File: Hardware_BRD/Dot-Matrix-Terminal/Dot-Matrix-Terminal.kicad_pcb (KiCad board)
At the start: 2 copper layers, 105 x 50 mm, 62 parts, among them J1 USB_B, J2 Conn_01x17, J3 Conn_01x10, J4 Conn_01x02, J5 Barrel_Jack, J6 Conn_01x02, J7 Conn_01x02, J8 Conn_01x02, Q1 IRLML0030, Q10 IRLML0030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

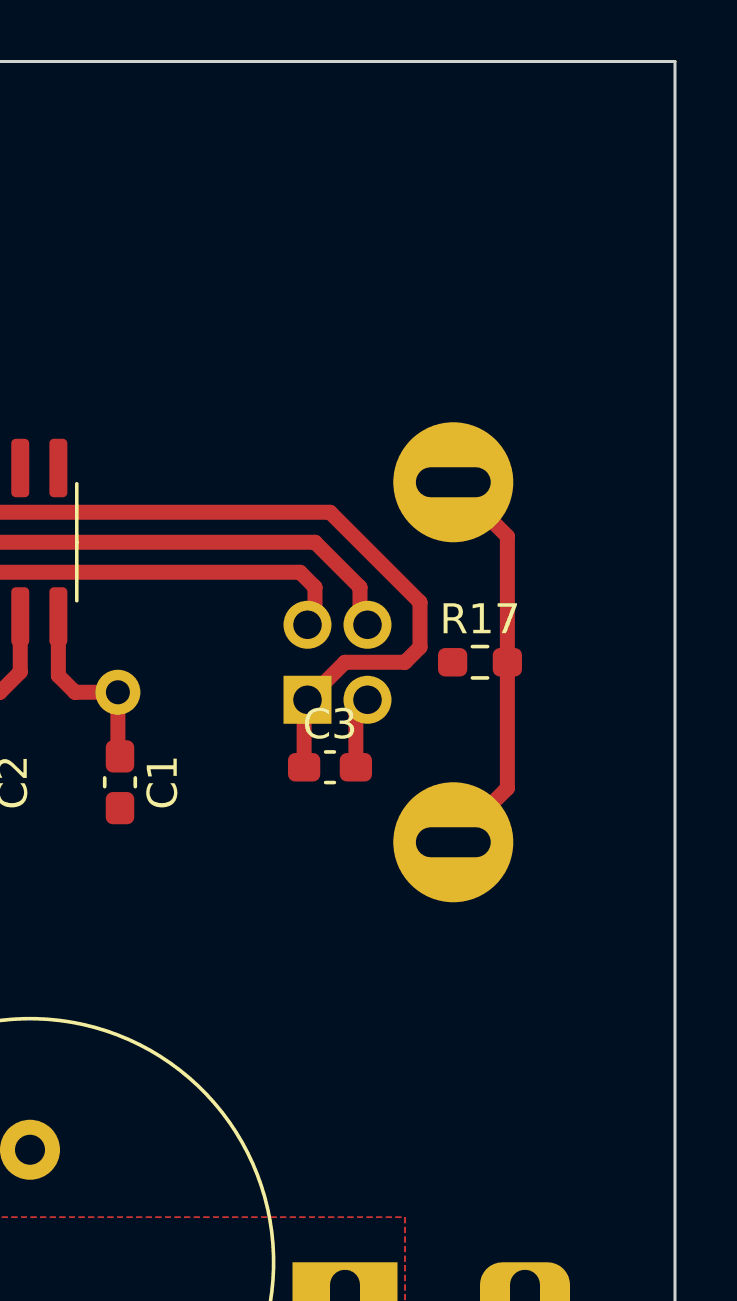
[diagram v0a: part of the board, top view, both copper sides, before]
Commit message: Couple of mounting holes added
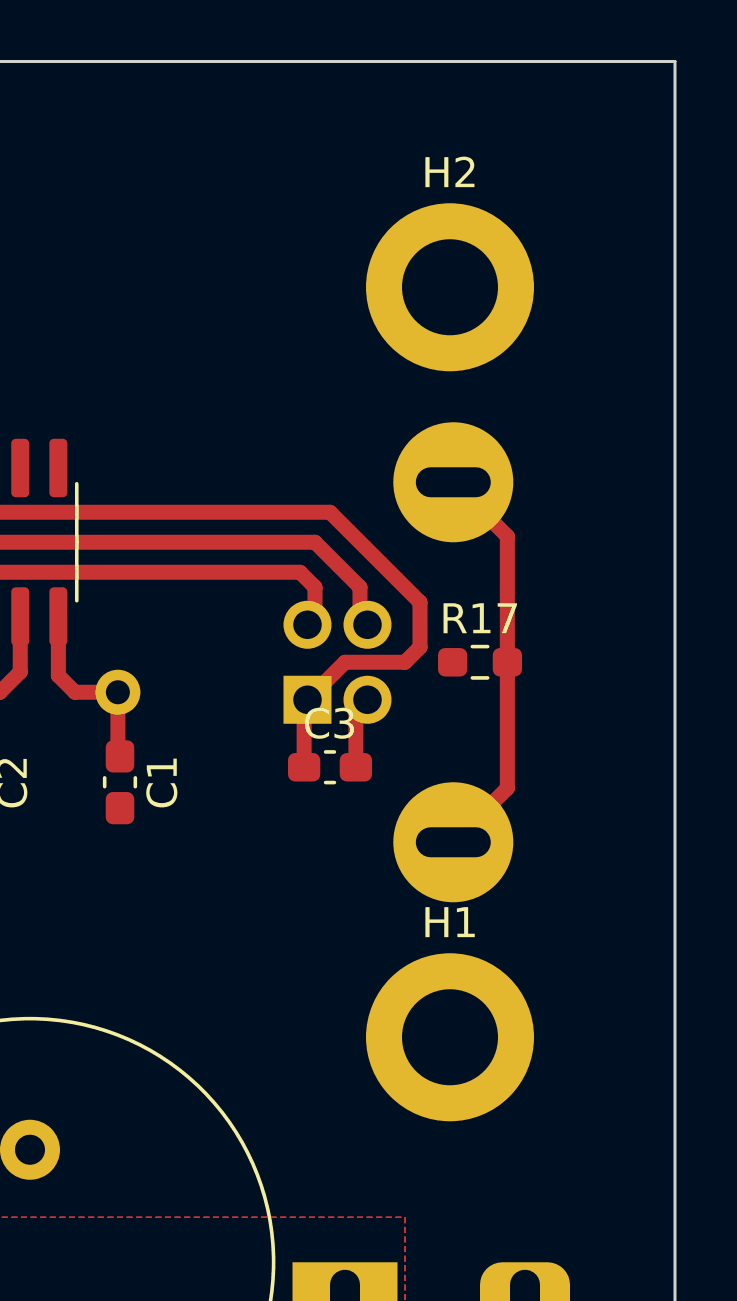
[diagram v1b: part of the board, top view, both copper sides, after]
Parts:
- added H1: MountingHole_Pad, MountingHole:MountingHole_3.2mm_M3_DIN965_Pad, F.Cu at (197.5, 132.5)
- added H2: MountingHole_Pad, MountingHole:MountingHole_3.2mm_M3_DIN965_Pad, F.Cu at (197.5, 107.5)
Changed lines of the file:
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@@
     )
+  )
+  (footprint "MountingHole:MountingHole_3.2mm_M3_DIN965_Pad" (layer "F.Cu")
+    (at 197.5 132.5)
+    (descr "Mounting Hole 3.2mm, M3, DIN965")
+    (tags "mounting hole 3.2mm m3 din965")
+    (property "Sheetfile" "Dot-Matrix-Terminal.kicad_sch")
+    (property "Sheetname" "")
+    (property "ki_description" "Mounting Hole with connection")
+    (property "ki_keywords" "mounting hole")
+    (attr exclude_from_pos_files)
+    (fp_text reference "H1" (at 0 -3.8) (layer "F.SilkS")
+        (effects (font (size 1 1) (thickness 0.15)))
+    )
+    (fp_text value "MountingHole_Pad" (at 0 3.8) (layer "F.Fab")
+        (effects (font (size 1 1) (thickness 0.15)))
+    )
+    (fp_text user "${REFERENCE}" (at 0 0) (layer "F.Fab")
+        (effects (font (size 1 1) (thickness 0.15)))
+    )
+    (fp_circle (center 0 0) (end 2.8 0)
+      (stroke (width 0.15) (type solid)) (fill none) (layer "Cmts.User"))
+    (fp_circle (center 0 0) (end 3.05 0)
+      (stroke (width 0.05) (type solid)) (fill none) (layer "F.CrtYd"))
+    (pad "1" thru_hole circle (at 0 0) (size 5.6 5.6) (drill 3.2) (layers "*.Cu" "*.Mask")
+      (net 2 "GND") (pinfunction "1") (pintype "input"))
   )
   (footprint "RF_Module:ESP32-WROOM-32" (layer "F.Cu")
@@
     )
   )
+  (footprint "MountingHole:MountingHole_3.2mm_M3_DIN965_Pad" (layer "F.Cu")
+    (at 197.5 107.5)
+    (descr "Mounting Hole 3.2mm, M3, DIN965")
+    (tags "mounting hole 3.2mm m3 din965")
+    (property "Sheetfile" "Dot-Matrix-Terminal.kicad_sch")
+    (property "Sheetname" "")
+    (property "ki_description" "Mounting Hole with connection")
+    (property "ki_keywords" "mounting hole")
+    (attr exclude_from_pos_files)
+    (fp_text reference "H2" (at 0 -3.8) (layer "F.SilkS")
+        (effects (font (size 1 1) (thickness 0.15)))
+    )
+    (fp_text value "MountingHole_Pad" (at 0 3.8) (layer "F.Fab")
+        (effects (font (size 1 1) (thickness 0.15)))
+    )
+    (fp_text user "${REFERENCE}" (at 0 0) (layer "F.Fab")
+        (effects (font (size 1 1) (thickness 0.15)))
+    )
+    (fp_circle (center 0 0) (end 2.8 0)
+      (stroke (width 0.15) (type solid)) (fill none) (layer "Cmts.User"))
+    (fp_circle (center 0 0) (end 3.05 0)
+      (stroke (width 0.05) (type solid)) (fill none) (layer "F.CrtYd"))
+    (pad "1" thru_hole circle (at 0 0) (size 5.6 5.6) (drill 3.2) (layers "*.Cu" "*.Mask")
+      (net 2 "GND") (pinfunction "1") (pintype "input"))
+  )
   (footprint "Package_TO_SOT_SMD:SOT-23_Handsoldering" (layer "F.Cu")

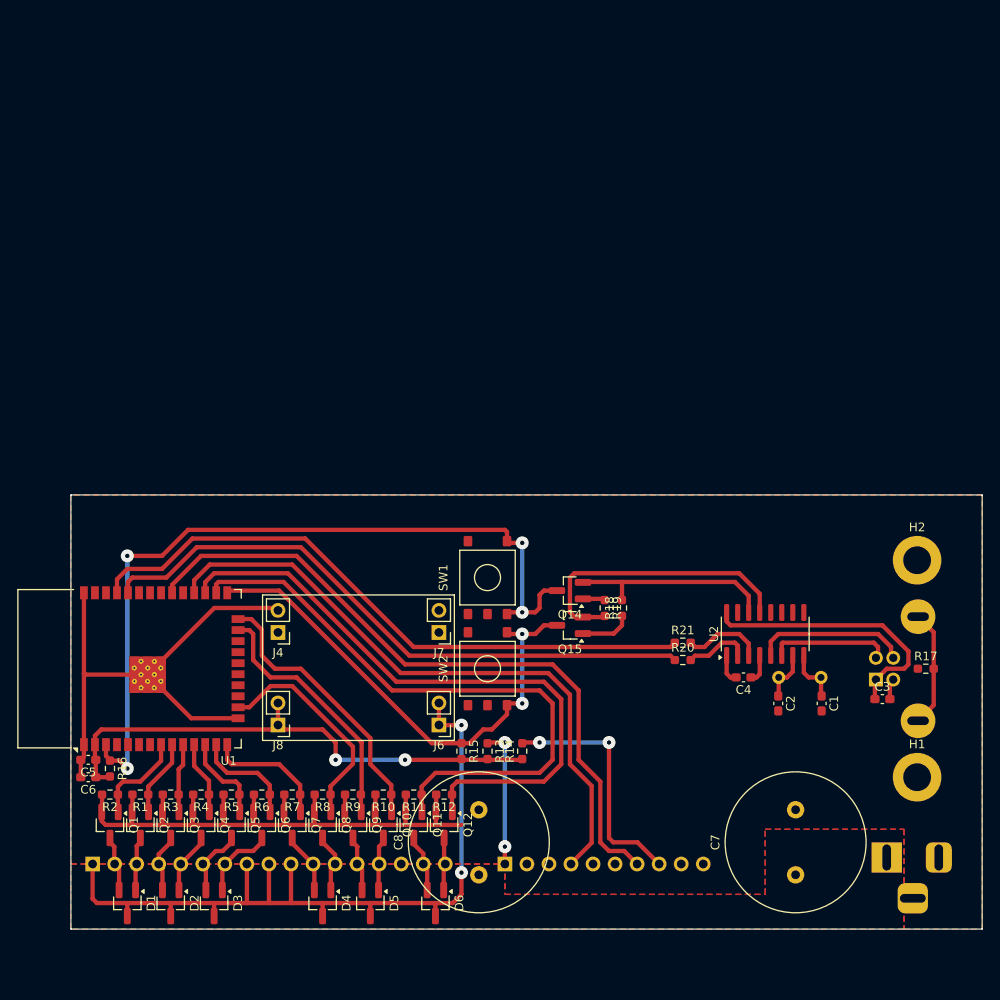
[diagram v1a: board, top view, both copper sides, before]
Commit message: Rotated board since FlatCAM can not do it properly(
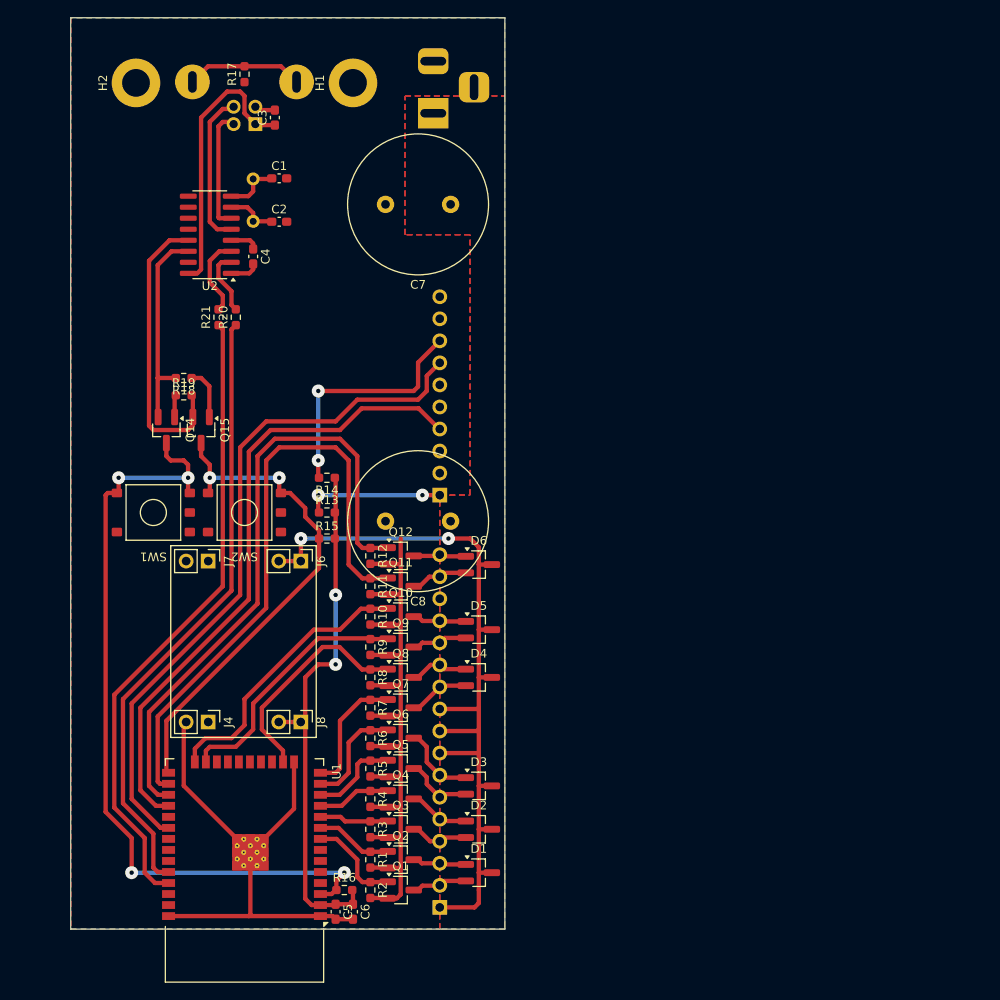
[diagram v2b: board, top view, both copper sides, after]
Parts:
- moved H2 105.5 mm to (107.5, 52.5), turned to 90 degrees
- moved R17 104.2 mm to (120.0, 51.5), turned to 90 degrees
- moved H1 103.1 mm to (132.5, 52.5), turned to 90 degrees
- moved J5 100.4 mm to (141.8, 56.0), turned to -90 degrees
- moved C3 96.9 mm to (123.5, 56.5), turned to 90 degrees
- moved J1 96.0 mm to (121.2, 57.2), turned to 90 degrees
- moved C1 87.0 mm to (124.0, 63.5), turned to 0 degrees
- moved C7 86.9 mm to (143.8, 66.5), turned to 180 degrees
- moved Y1 80.2 mm to (121.0, 68.4), turned to 90 degrees
- moved C2 79.9 mm to (124.0, 68.5), turned to 0 degrees
- moved U2 78.8 mm to (116.0, 70.0), turned to 180 degrees
- moved C4 74.5 mm to (121.0, 72.5), turned to -90 degrees
- moved R21 65.3 mm to (117.0, 79.5), turned to 90 degrees
- moved R20 64.9 mm to (119.0, 79.5), turned to 90 degrees
- moved R18 57.0 mm to (113.0, 86.5), turned to 180 degrees
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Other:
- board size 105 x 50 mm -> 50 x 105 mm
